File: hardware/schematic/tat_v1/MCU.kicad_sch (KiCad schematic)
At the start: 23 parts, among them J1 JST-SH 1x7P, SW1 SW_SPDT, SW2 SW_Push, U1 STM32U073CCUx, X1 32.768KHz

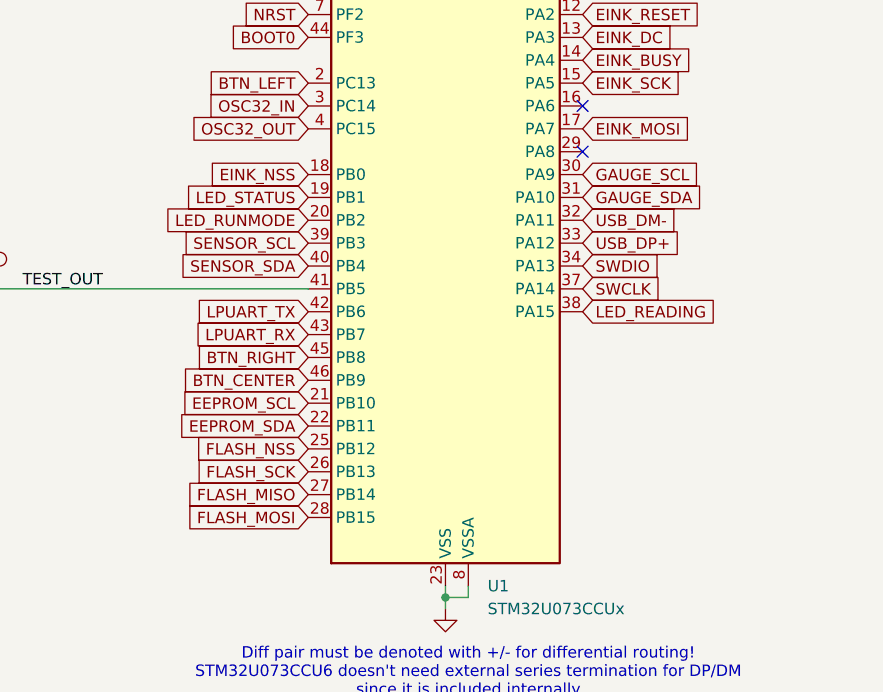
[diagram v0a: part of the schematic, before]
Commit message: Simplified partslist and working on updated schematic
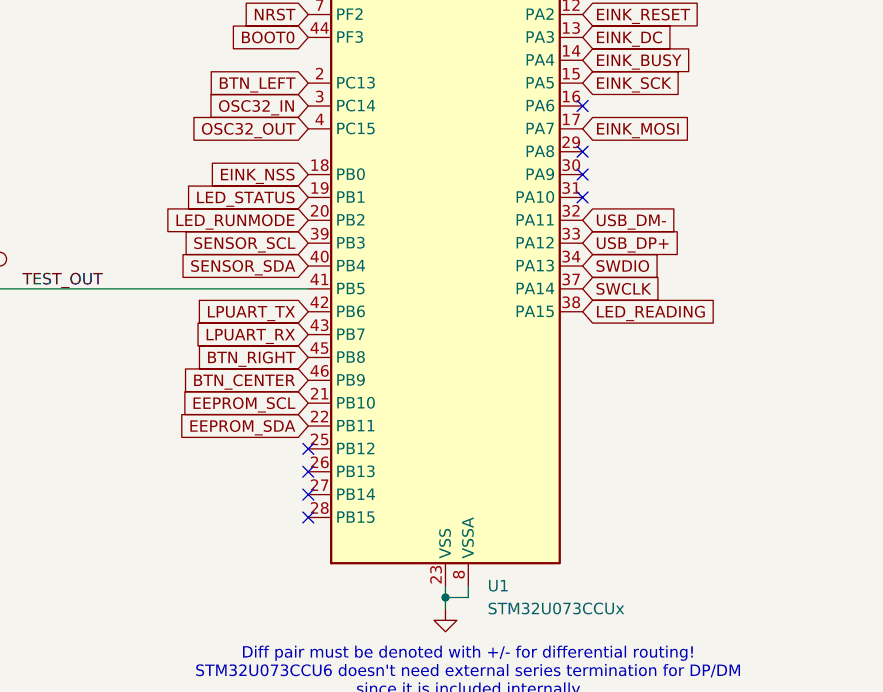
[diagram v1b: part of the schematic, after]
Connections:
- net FLASH_MISO: no longer names the net of U1.27 (PB14)
- net FLASH_MOSI: no longer names the net of U1.28 (PB15)
- net FLASH_NSS: no longer names the net of U1.25 (PB12)
- net FLASH_SCK: no longer names the net of U1.26 (PB13)
- net GAUGE_SCL: no longer names the net of U1.30 (PA9)
- net GAUGE_SDA: no longer names the net of U1.31 (PA10)
- no-connect marks 6 -> 12

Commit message: Basic circuit is complete, needs double checking
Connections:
- net STAT2: now reaches U1.28 (PB15)
- net STAT1: now reaches U1.29 (PA8)
- net USB Sense: now reaches U1.30 (PA9)
- net BTN_CENTER renamed Center Button
- net BTN_LEFT renamed Left Button
- net BTN_RIGHT renamed Right Button
- net EEPROM_SCL renamed EEPROM SCL
- net EEPROM_SDA renamed EEPROM SDA
- net EINK_BUSY renamed EInk Busy
- net EINK_DC renamed EInk DC
- net EINK_MOSI renamed EInk SDA
- net EINK_NSS renamed ~{EInk SS}
- net EINK_RESET renamed ~{EInk Reset}
- net EINK_SCK renamed EInk SCL
- net LED_READING renamed Reading LED
- net LED_RUNMODE renamed Runmode LED
- net LED_STATUS renamed Status LED
- net LPUART_RX renamed LPUART RX
- net LPUART_TX renamed LPUART TX
- net NRST renamed ~{RESET}
- net OSC32_IN renamed OSC32 In
- net OSC32_OUT renamed OSC32 Out
- net SENSOR_SCL renamed Sensor SCL
- net SENSOR_SDA renamed Sensor SDA
- net USB_DM- renamed USB_D-
- net USB_DP+ renamed USB_D+
- no-connect marks 12 -> 9
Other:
- moved on the sheet: D1, D2, D3, J1, R2, R3, R4

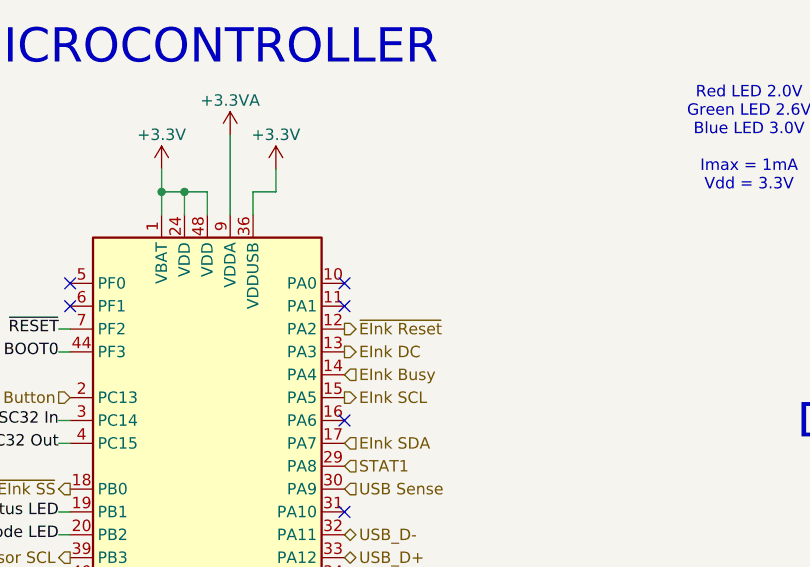
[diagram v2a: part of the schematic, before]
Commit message: Added measuring battery voltage using the ADC. Basic schematic is complete, needs checking and refinement
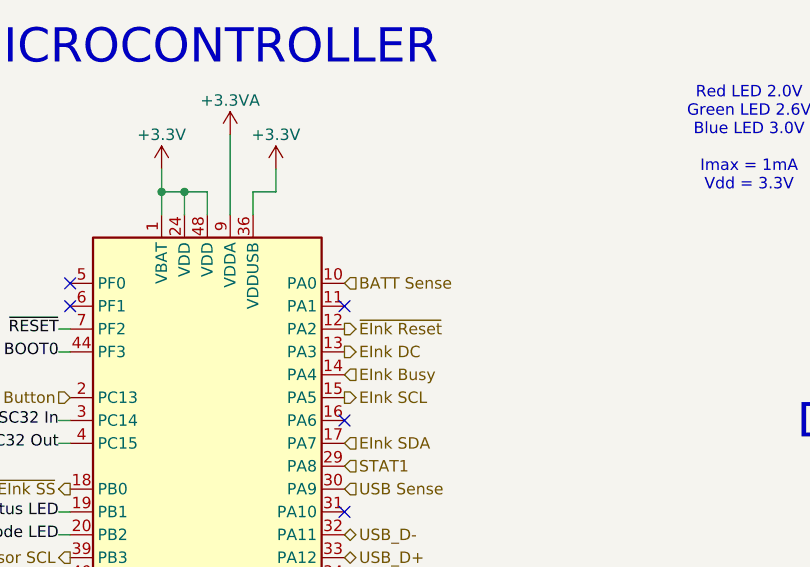
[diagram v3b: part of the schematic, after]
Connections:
- net BATT Sense: now reaches U1.10 (PA0)
- no-connect marks 9 -> 8
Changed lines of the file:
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@@
 		(at 168.91 92.71)
-	)
-	(no_connect
-		(at 168.91 67.31)
 	)
 	(wire
@@
 		)
 	)
+	(hierarchical_label "BATT Sense"
+		(shape input)
+		(at 168.91 67.31 0)
+		(effects
+			(font
+				(size 1.27 1.27)
+			)
+			(justify left)
+		)
+	)

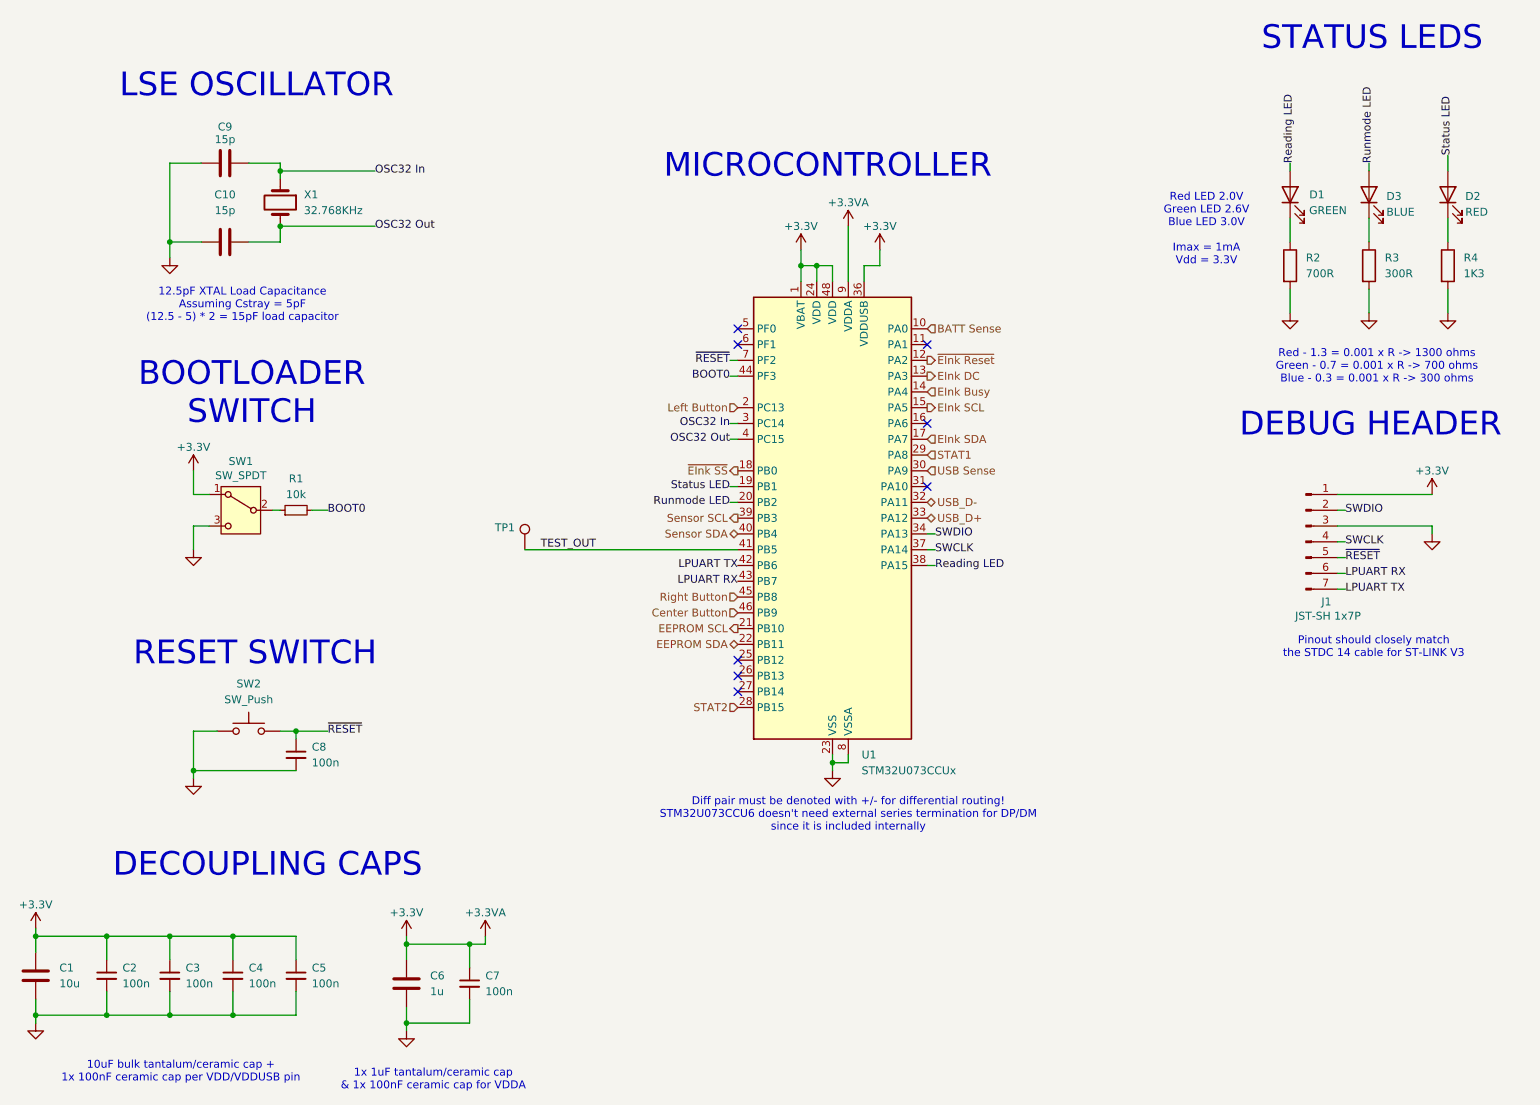
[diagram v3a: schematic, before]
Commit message: Cleaned up basic schematic and double checked all components. Need to complete ERC.
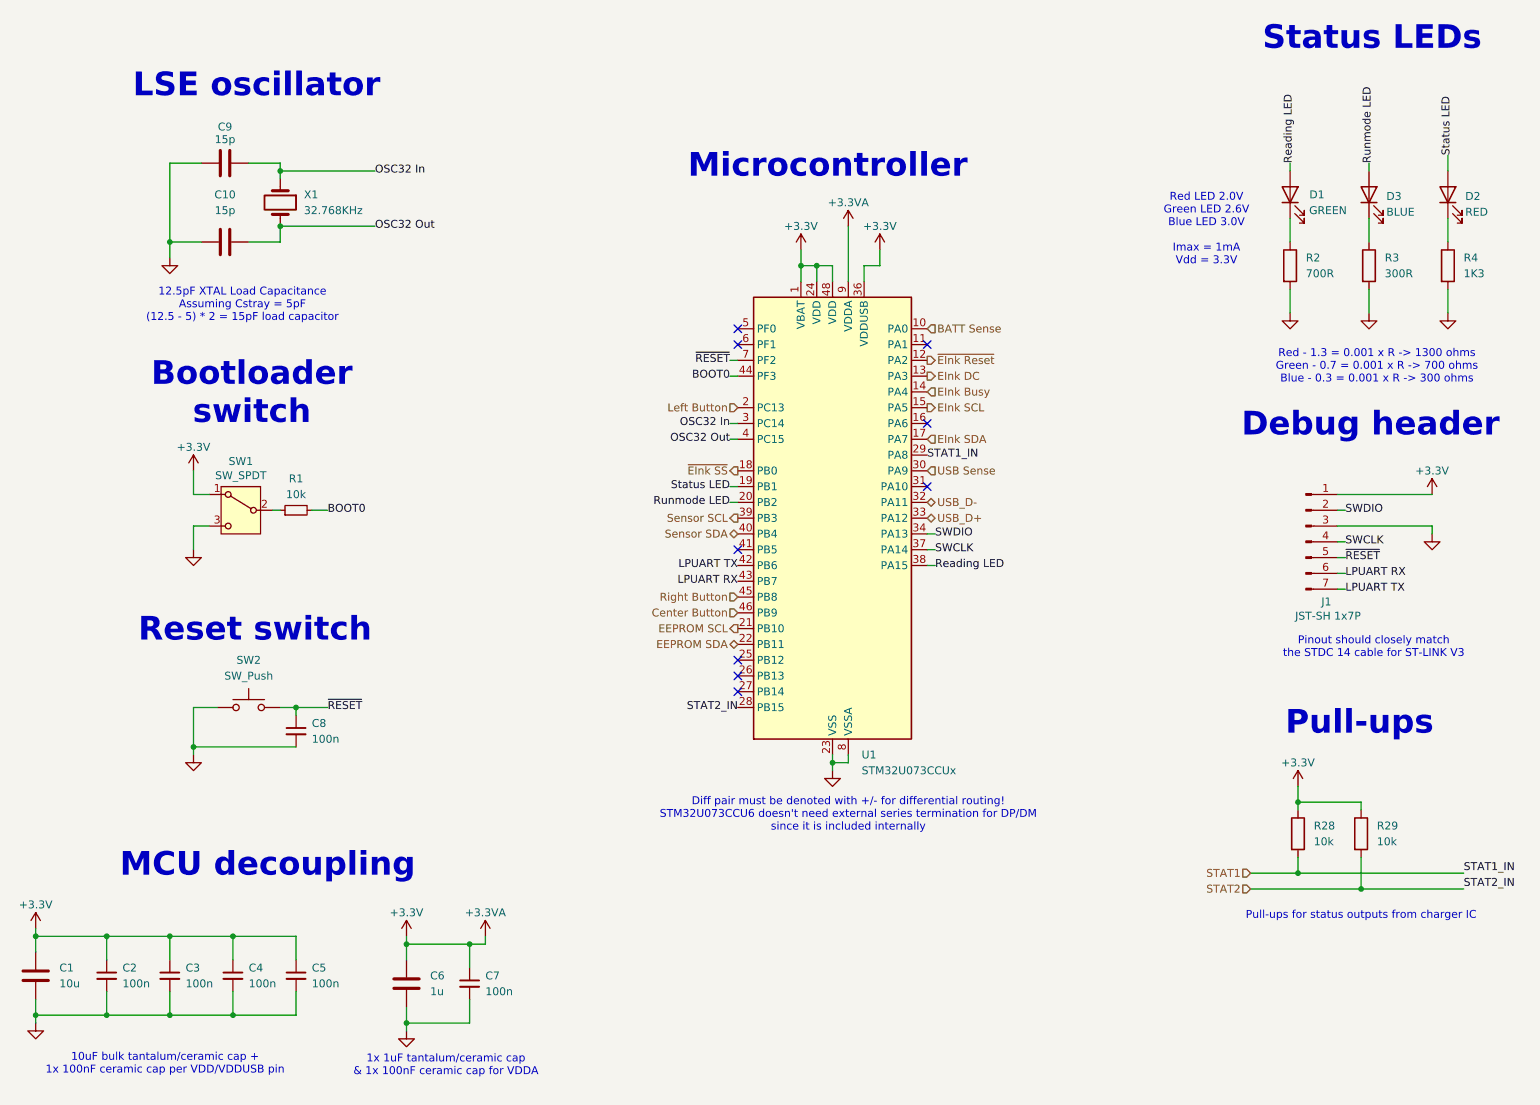
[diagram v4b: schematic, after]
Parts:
- removed TP1: TestPoint, symbol Connector:TestPoint
- added R28, R29: 10k, symbol Device:R
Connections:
- net +3.3V: now also R28.1, R29.1
- net STAT1: now also R28.2
- net STAT2: now also R29.2
- net TEST_OUT: no longer names the net of U1.41 (PB5)
- no-connect marks 8 -> 9
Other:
- note added: "Bootloader switch"
- note added: "Debug header"
- note added: "LSE oscillator"
- note added: "MCU decoupling"
- note added: "Microcontroller"
- note added: "Pull-ups"
- note added: "Pull-ups for status outputs from charger IC"
- note added: "Reset switch"
- note added: "Status LEDs"
- note removed: "BOOTLOADER SWITCH"
- note removed: "DEBUG HEADER"
- note removed: "DECOUPLING CAPS"
- note removed: "LSE OSCILLATOR"
- note removed: "MICROCONTROLLER"
- note removed: "RESET SWITCH"
- note removed: "STATUS LEDS"
- moved on the sheet: C8, SW2

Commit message: Added new titles to sheets
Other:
- title: (none) -> Tiny Ambient Tracker - microcontroller
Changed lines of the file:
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@@
 	(generator_version "9.0")
 	(paper "A4")
+	(title_block
+		(title "Tiny Ambient Tracker - microcontroller")
+	)
 	(text "LSE oscillator"
 		(exclude_from_sim no)

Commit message: Used auto reference designator on whole schematic
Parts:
- renumbered C2 to C10, C3 to C11, C9 to C12, C10 to C13, C4 to C14, C8 to C15, C5 to C16, C6 to C17, C7 to C18, C1 to C9, D3 to D2, D2 to D3, J1 to J3, R1 to R12, R2 to R13, R28 to R14, R29 to R15, R3 to R16, R4 to R17, SW1 to SW2, SW2 to SW3, U1 to U4

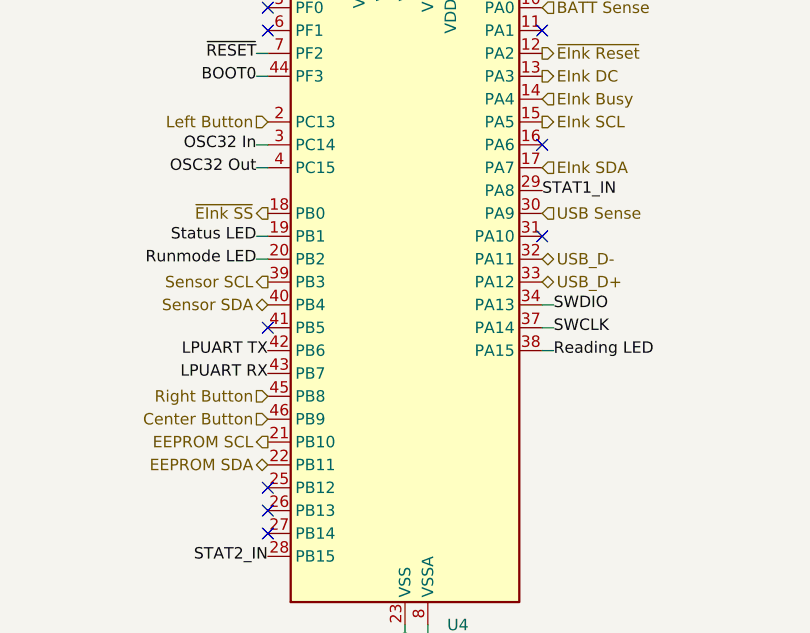
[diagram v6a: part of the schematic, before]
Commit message: Synced hierarchical pins to sheets, need to fix rest of ERC errors
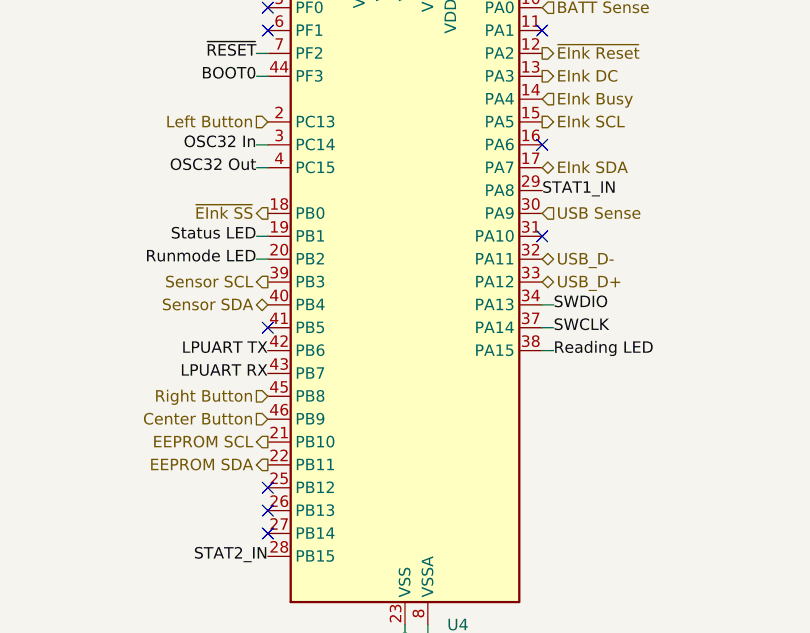
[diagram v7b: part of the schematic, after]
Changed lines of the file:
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@@
 	)
 	(hierarchical_label "EInk SDA"
-		(shape input)
+		(shape bidirectional)
 		(at 168.91 85.09 0)
 		(effects
@@
 	)
 	(hierarchical_label "EEPROM SDA"
-		(shape bidirectional)
+		(shape output)
 		(at 138.43 118.11 180)
 		(effects
